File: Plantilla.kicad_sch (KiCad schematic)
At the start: 12 parts, among them J1 Screw_Terminal_01x03, Q1 IRF540N, U1 TIMER 555

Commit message: Cambio nombre
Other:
- note added: "DIMMER 5"
- note removed: "DIMMER 555"
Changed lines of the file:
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@@
 		(company "UPNA")
 	)
-	(text "DIMMER 555"
+	(text "DIMMER 5"
 		(exclude_from_sim no)
 		(at 151.13 45.212 0)

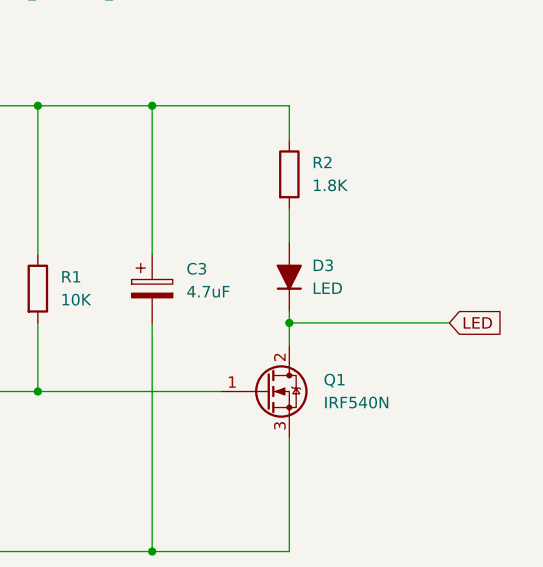
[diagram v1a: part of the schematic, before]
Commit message: Añadido nuevo LED en paralelo
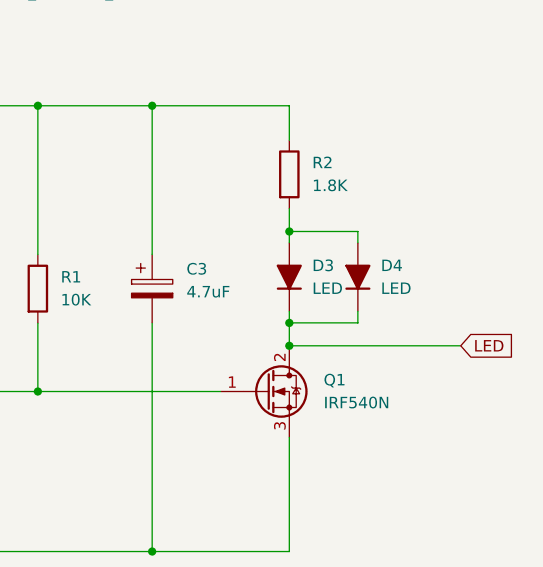
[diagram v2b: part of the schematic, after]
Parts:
- added D4: LED, Diode_SMD:D_1206_3216Metric, symbol Device:D_Filled
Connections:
- net LED: now also D4.1 (K)
- net at D3.2 (A), R2.2: now also D4.2 (A)
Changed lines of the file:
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@@
+	)
+	(junction
+		(at 201.93 120.65)
+		(diameter 0)
+		(color 0 0 0 0)
 	)
 	(junction
@@
 	)
 	(junction
+		(at 201.93 107.95)
+		(diameter 0)
+		(color 0 0 0 0)
+	)
+	(junction
 		(at 113.03 143.51)
 		(diameter 0)
@@
 	(wire
 		(pts
-			(xy 201.93 105.41) (xy 201.93 109.22)
+			(xy 209.55 116.84) (xy 209.55 118.11)
+		)
+		(stroke
+			(width 0)
+			(type default)
+		)
+	)
+	(wire
+		(pts
+			(xy 201.93 105.41) (xy 201.93 107.95)
 		)
 		(stroke
@@
 	(wire
 		(pts
-			(xy 201.93 118.11) (xy 219.71 118.11)
+			(xy 201.93 120.65) (xy 220.98 120.65)
 		)
 		(stroke
@@
 	(wire
 		(pts
+			(xy 209.55 118.11) (xy 201.93 118.11)
+		)
+		(stroke
+			(width 0)
+			(type default)
+		)
+	)
+	(wire
+		(pts
 			(xy 113.03 125.73) (xy 113.03 133.35)
 		)
@@
 	(wire
 		(pts
+			(xy 209.55 107.95) (xy 209.55 109.22)
+		)
+		(stroke
+			(width 0)
+			(type default)
+		)
+	)
+	(wire
+		(pts
 			(xy 124.46 130.81) (xy 128.27 130.81)
 		)
@@
 	(wire
 		(pts
+			(xy 201.93 118.11) (xy 201.93 120.65)
+		)
+		(stroke
+			(width 0)
+			(type default)
+		)
+	)
+	(wire
+		(pts
 			(xy 138.43 93.98) (xy 140.97 93.98)
 		)
@@
 	(wire
 		(pts
+			(xy 153.67 125.73) (xy 173.99 125.73)
+		)
+		(stroke
+			(width 0)
+			(type default)
+		)
+	)
+	(wire
+		(pts
+			(xy 201.93 109.22) (xy 201.93 107.95)
+		)
+		(stroke
+			(width 0)
+			(type default)
+		)
+	)
+	(wire
+		(pts
+			(xy 102.87 96.52) (xy 102.87 106.68)
+		)
+		(stroke
+			(width 0)
+			(type default)
+		)
+	)
+	(wire
+		(pts
+			(xy 128.27 120.65) (xy 120.65 120.65)
+		)
+		(stroke
+			(width 0)
+			(type default)
+		)
+	)
+	(wire
+		(pts
+			(xy 201.93 107.95) (xy 209.55 107.95)
+		)
+		(stroke
+			(width 0)
+			(type default)
+		)
+	)
+	(wire
+		(pts
+			(xy 201.93 143.51) (xy 186.69 143.51)
+		)
+		(stroke
+			(width 0)
+			(type default)
+		)
+	)
+	(wire
+		(pts
+			(xy 153.67 120.65) (xy 158.75 120.65)
+		)
+		(stroke
+			(width 0)
+			(type default)
+		)
+	)
+	(wire
+		(pts
+			(xy 186.69 143.51) (xy 186.69 118.11)
+		)
+		(stroke
+			(width 0)
+			(type default)
+		)
+	)
+	(wire
+		(pts
+			(xy 140.97 135.89) (xy 140.97 143.51)
+		)
+		(stroke
+			(width 0)
+			(type default)
+		)
+	)
+	(wire
+		(pts
+			(xy 186.69 93.98) (xy 201.93 93.98)
+		)
+		(stroke
+			(width 0)
+			(type default)
+		)
+	)
+	(wire
+		(pts
+			(xy 186.69 93.98) (xy 186.69 110.49)
+		)
+		(stroke
+			(width 0)
+			(type default)
+		)
+	)
+	(wire
+		(pts
 			(xy 201.93 116.84) (xy 201.93 118.11)
-		)
-		(stroke
-			(width 0)
-			(type default)
-		)
-	)
-	(wire
-		(pts
-			(xy 153.67 125.73) (xy 173.99 125.73)
-		)
-		(stroke
-			(width 0)
-			(type default)
-		)
-	)
-	(wire
-		(pts
-			(xy 102.87 96.52) (xy 102.87 106.68)
-		)
-		(stroke
-			(width 0)
-			(type default)
-		)
-	)
-	(wire
-		(pts
-			(xy 128.27 120.65) (xy 120.65 120.65)
-		)
-		(stroke
-			(width 0)
-			(type default)
-		)
-	)
-	(wire
-		(pts
-			(xy 201.93 143.51) (xy 186.69 143.51)
-		)
-		(stroke
-			(width 0)
-			(type default)
-		)
-	)
-	(wire
-		(pts
-			(xy 153.67 120.65) (xy 158.75 120.65)
-		)
-		(stroke
-			(width 0)
-			(type default)
-		)
-	)
-	(wire
-		(pts
-			(xy 186.69 143.51) (xy 186.69 118.11)
-		)
-		(stroke
-			(width 0)
-			(type default)
-		)
-	)
-	(wire
-		(pts
-			(xy 140.97 135.89) (xy 140.97 143.51)
-		)
-		(stroke
-			(width 0)
-			(type default)
-		)
-	)
-	(wire
-		(pts
-			(xy 186.69 93.98) (xy 201.93 93.98)
-		)
-		(stroke
-			(width 0)
-			(type default)
-		)
-	)
-	(wire
-		(pts
-			(xy 186.69 93.98) (xy 186.69 110.49)
-		)
-		(stroke
-			(width 0)
-			(type default)
-		)
-	)
-	(wire
-		(pts
-			(xy 201.93 118.11) (xy 201.93 120.65)
 		)
 		(stroke
@@
 	(global_label "LED"
 		(shape input)
-		(at 219.71 118.11 0)
+		(at 220.98 120.65 0)
 		(fields_autoplaced yes)
 		(effects
@@
 		)
 		(property "Intersheetrefs" "${INTERSHEET_REFS}"
-			(at 226.1423 118.11 0)
+			(at 227.4123 120.65 0)
 			(hide yes)
 			(show_name no)
@@
 					(unit 1)
 				)
+			)
+		)
+	)
+	(symbol
+		(lib_id "Device:D_Filled")
+		(at 209.55 113.03 90)
+		(unit 1)
+		(body_style 1)
+		(exclude_from_sim no)
+		(in_bom yes)
+		(on_board yes)
+		(in_pos_files yes)
+		(dnp no)
+		(fields_autoplaced yes)
+		(property "Reference" "D4"
+			(at 212.09 111.7599 90)
+			(show_name no)
+			(do_not_autoplace no)
+			(effects
+				(font
+					(size 1.27 1.27)
+				)
+				(justify right)
+			)
+		)
+		(property "Value" "LED"
+			(at 212.09 114.2999 90)
+			(show_name no)
+			(do_not_autoplace no)
+			(effects
+				(font
+					(size 1.27 1.27)
+				)
+				(justify right)
+			)
+		)
+		(property "Footprint" "Diode_SMD:D_1206_3216Metric"
+			(at 209.55 113.03 0)
+			(hide yes)
+			(show_name no)
+			(do_not_autoplace no)
+			(effects
+				(font
+					(size 1.27 1.27)
+				)
+			)
+		)
+		(property "Datasheet" ""
+			(at 209.55 113.03 0)
+			(hide yes)
+			(show_name no)
+			(do_not_autoplace no)
+			(effects
+				(font
+					(size 1.27 1.27)
+				)
+			)
+		)
+		(property "Description" "Diode, filled shape"
+			(at 209.55 113.03 0)
+			(hide yes)
+			(show_name no)
+			(do_not_autoplace no)
+			(effects
+				(font
+					(size 1.27 1.27)
+				)
+			)
+		)
+		(property "Sim.Device" "D"
+			(at 209.55 113.03 0)
+			(hide yes)
+			(show_name no)
+			(do_not_autoplace no)
+			(effects
+				(font
+					(size 1.27 1.27)
+				)
+			)
+		)
+		(property "Sim.Pins" "1=K 2=A"
+			(at 209.55 113.03 0)
+			(hide yes)
+			(show_name no)
+			(do_not_autoplace no)
+			(effects
+				(font
+					(size 1.27 1.27)
+				)
+			)
+		)
+		(pin "2"
+		)
+		(pin "1"
+		)
+		(instances
+			(project "Plantilla"
+				(path "/6a55d53f-e3c4-4300-a1b7-a7f79b9491fb"
+					(reference "D4")
+					(unit 1)
+				)
